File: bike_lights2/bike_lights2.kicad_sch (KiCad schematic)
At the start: 35 parts, among them J2 LED, J3 B+, P1 USB_C_Plug_USB2.0, U1 TL431DBZ, U3 MIC2289, U4 MCP6002-xMS, U5 MCP73831-2-ADI/OT

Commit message: a
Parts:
- removed H1: MountingHole_Pad, Connector_Wire:SolderWirePad_1x01_SMD_5x10mm, symbol Mechanical:MountingHole_Pad
- added C10: 10u, Capacitor_SMD:C_0603_1608Metric, symbol Device:C
- added SW1: TL49, footprints:TL49PO, symbol Switch:SW_DPDT_x2
- C7: footprint Capacitor_SMD:C_0805_2012Metric_Pad1.18x1.45mm_HandSolder -> Capacitor_SMD:C_0603_1608Metric
- L1: value 10µ -> 6.8µ; footprint footprints:DO1813H -> footprints:EPL2014_2x2mm_inductor_Coilcraft
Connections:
- net +BATT: now also SW1.3 (C), SW1.6 (C); no longer D1.2 (A), J3.1 (Pin_1), U5.3 (V_{BAT})
- net GND: now also C10.2
- net Vusb: now also D1.2 (A)
- new net Battery: C10.1, J3.1 (Pin_1), SW1.2 (B), SW1.5 (B), U5.3 (V_{BAT})
- no-connect marks 2 -> 4
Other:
- note added: "EPL2014-682"
- note removed: "DO1813H-103ML"
- moved on the sheet: C3, C4, C5, C6, C8, C9, D1, J2, J3, L1, R13, R15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

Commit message: a
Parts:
- added R1, R14: 5k1, Resistor_SMD:R_0603_1608Metric, symbol Device:R
- J2: footprint Connector_PinHeader_2.54mm:PinHeader_1x02_P2.54mm_Vertical -> footprints:JST_PH_1x02_P2.0-2.5mm_Vertical
- P1: symbol Connector:USB_C_Plug_USB2.0 -> Connector:USB_C_Receptacle_PowerOnly_6P
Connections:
- net GND: now also R1.1, R14.1; no longer P1.A1 (GND), P1.B1 (GND)
- net Vusb: no longer P1.A4 (VBUS), P1.B4 (VBUS)
- net CC1: now reaches P1.A5 (CC1)
- net CC1: now also R14.2
- net CC2: now reaches P1.B5 (CC2)
- net CC2: now also R1.2
- no-connect marks 4 -> 2

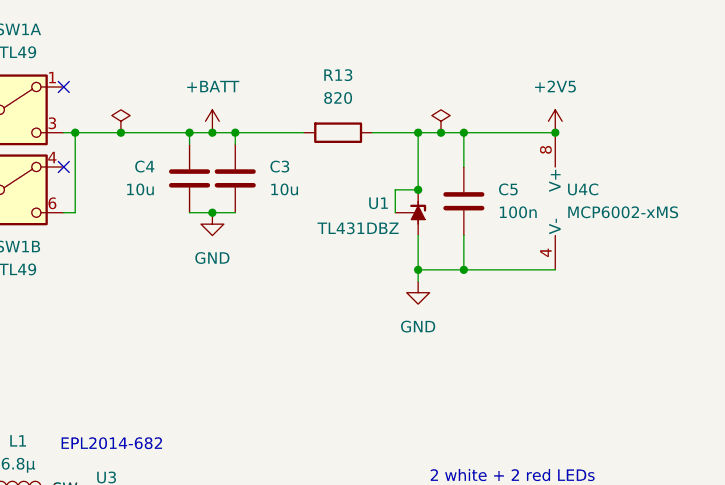
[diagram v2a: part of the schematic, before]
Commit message: update TL431 to T092
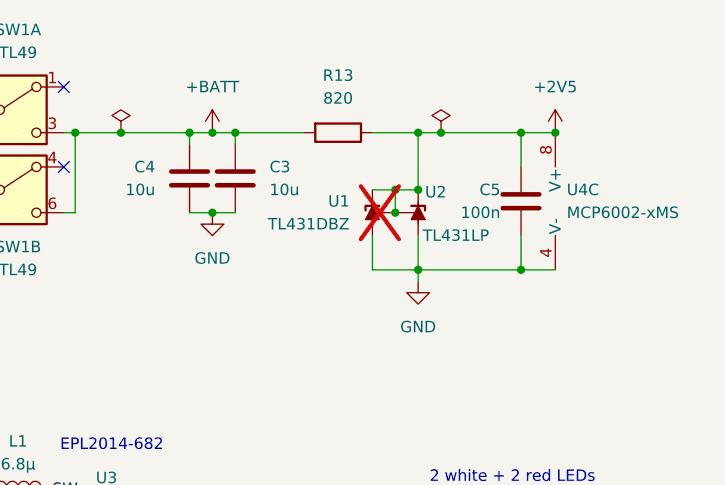
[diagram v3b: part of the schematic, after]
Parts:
- added U2: TL431LP, Package_TO_SOT_THT:TO-92_Inline, symbol Reference_Voltage:TL431LP
- U1: now not fitted
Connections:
- net +2V5: now also U2.1 (REF), U2.3 (K)
- net GND: now also U2.2 (A)
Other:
- moved on the sheet: C5
